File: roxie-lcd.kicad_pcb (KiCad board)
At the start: 2 copper layers, 7 parts, among them J1 Arduino-NANO-33, J2 VESC, J3 TFT, J4 BUTTON_1, J5 BUTTON_2, J6 BUTTON_3, J7 SD

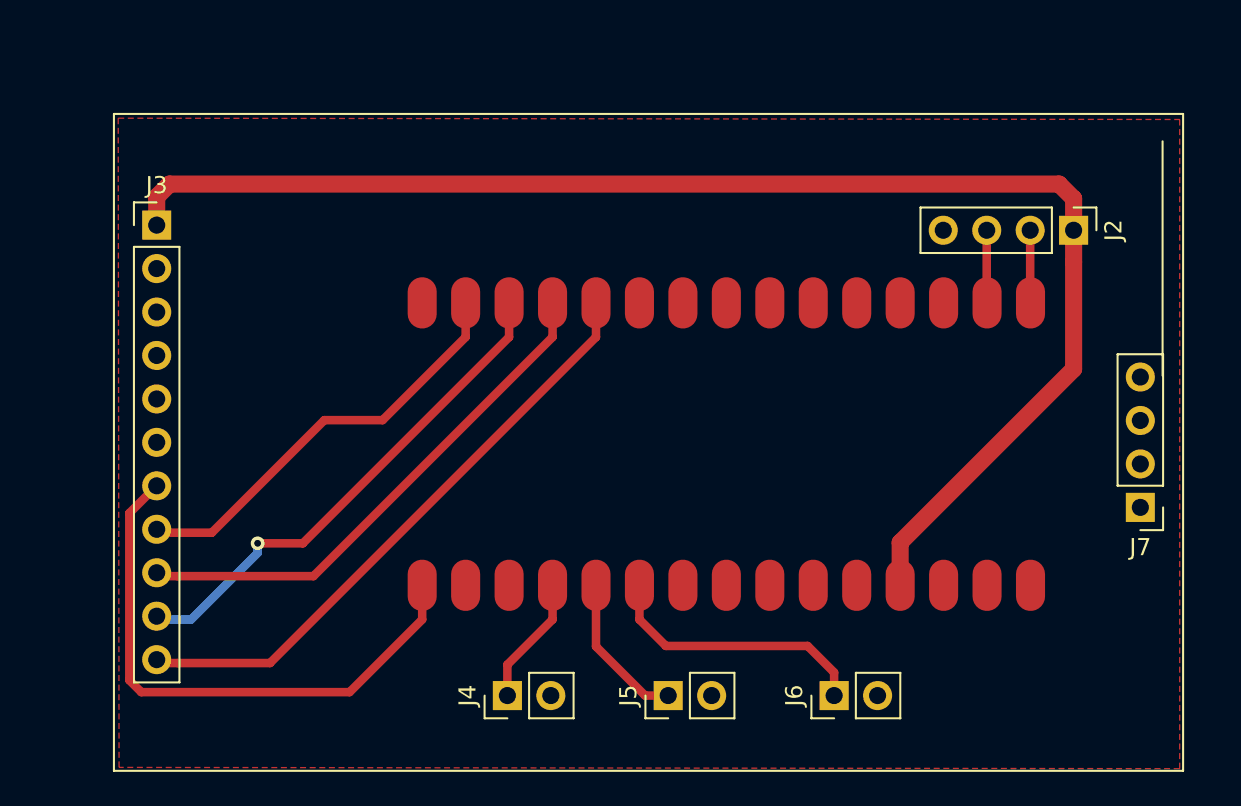
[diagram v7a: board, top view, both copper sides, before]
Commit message: added mountingholes on pcb, added PDF's of schematic and PCB
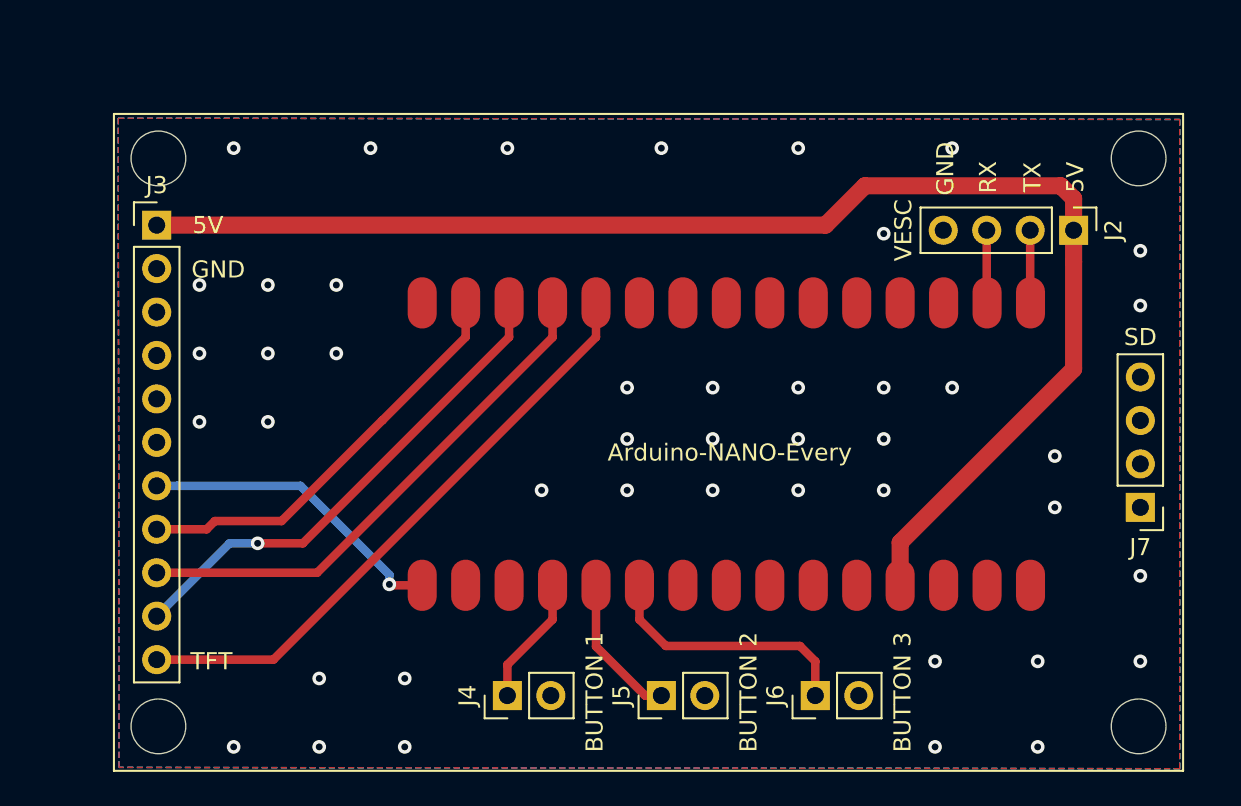
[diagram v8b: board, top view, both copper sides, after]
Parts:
- added H1: MountingHole, MountingHole:MountingHole_3.2mm_M3_ISO7380, F.Cu at (32.6, 32.6)
- added H2: M, MountingHole:MountingHole_3.2mm_M3_ISO7380, F.Cu at (32.6, 65.8)
- added H3: MountingHole, MountingHole:MountingHole_3.2mm_M3_ISO7380, F.Cu at (89.9, 32.6)
- added H4: M, MountingHole:MountingHole_3.2mm_M3_ISO7380, F.Cu at (89.9, 65.8)
- J1: value Arduino-NANO-33 -> Arduino-NANO-Every
- J4: value BUTTON_1 -> BUTTON 1
- J5: value BUTTON_2 -> BUTTON 2
- J6: value BUTTON_3 -> BUTTON 3
- moved J6 1.10 mm to (71.0, 64.0)
- moved J5 0.40 mm to (62.0, 64.0)
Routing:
- net CLK: track 33.2 -> 18.3 mm, vias 0 -> 1
- net 5V: track 82.9 -> 81.7 mm
- net BUTTON_3: track 16.0 -> 15.3 mm
- net GND: vias 0 -> 44
- added copper zone on B.Cu, net GND
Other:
- board text added: "5V"
- board text added: "GND"
- board text added: "RX"
- board text added: "TX"
